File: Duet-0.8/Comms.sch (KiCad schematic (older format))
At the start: 47 parts, among them J15 uSDHC, J19 ETHERNET, J22 USB, U10 SP2525A, U4 KSZ8051RNL, X1 CRYSTAL_4PIN

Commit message: USB B connector used.  Always-on fan connector added next to heater connector. Green power LED (5v) now has a bigger ballast resistor.
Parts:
- removed J22: USB, symbol USBCONN-MICROB
- removed R82: 0R, symbol R
- added J29: USB, symbol USB
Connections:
- net labels removed: UOTGID
- wire segments 179 -> 177
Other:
- moved on the sheet: C13, D3, R1, R3

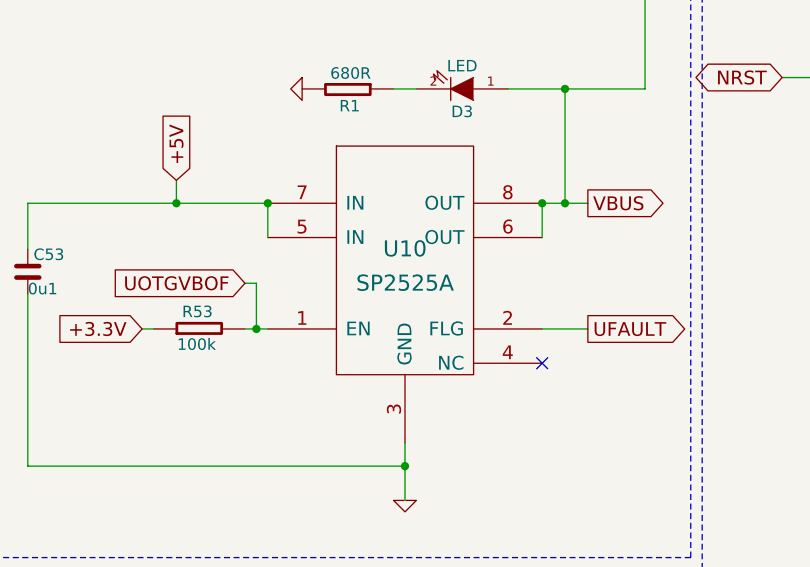
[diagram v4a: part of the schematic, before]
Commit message: SP2525A spec clarified to make it clear that the SP2525A-1 is the correct USB power chip.
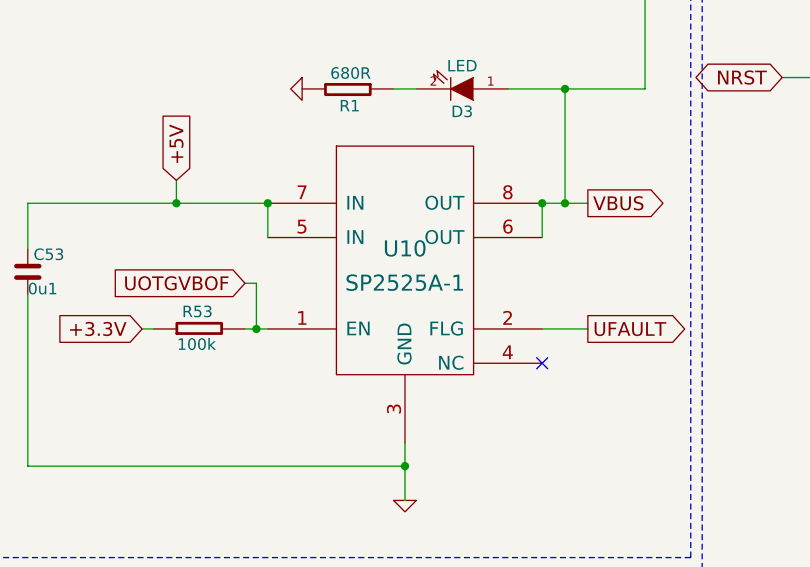
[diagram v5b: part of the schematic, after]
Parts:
- U10: value SP2525A -> SP2525A-1
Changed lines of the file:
@@
 Sheet 5 7
 Title "Duet"
-Date "9 jul 2015"
+Date "17 jul 2015"
 Rev "0.7"
 Comp "Think3DPrint3D, RepRapPro"
@@
 P 2400 3700
 F 0 "U10" H 2400 3750 70  0000 C CNN
-F 1 "SP2525A" H 2400 3600 70  0000 C CNN
+F 1 "SP2525A-1" H 2400 3600 70  0000 C CNN
 F 2 "" H 2400 3700 60  0001 C CNN
 F 3 "" H 2400 3700 60  0001 C CNN
